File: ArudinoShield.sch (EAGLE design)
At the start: 21 parts, among them IC1 L298

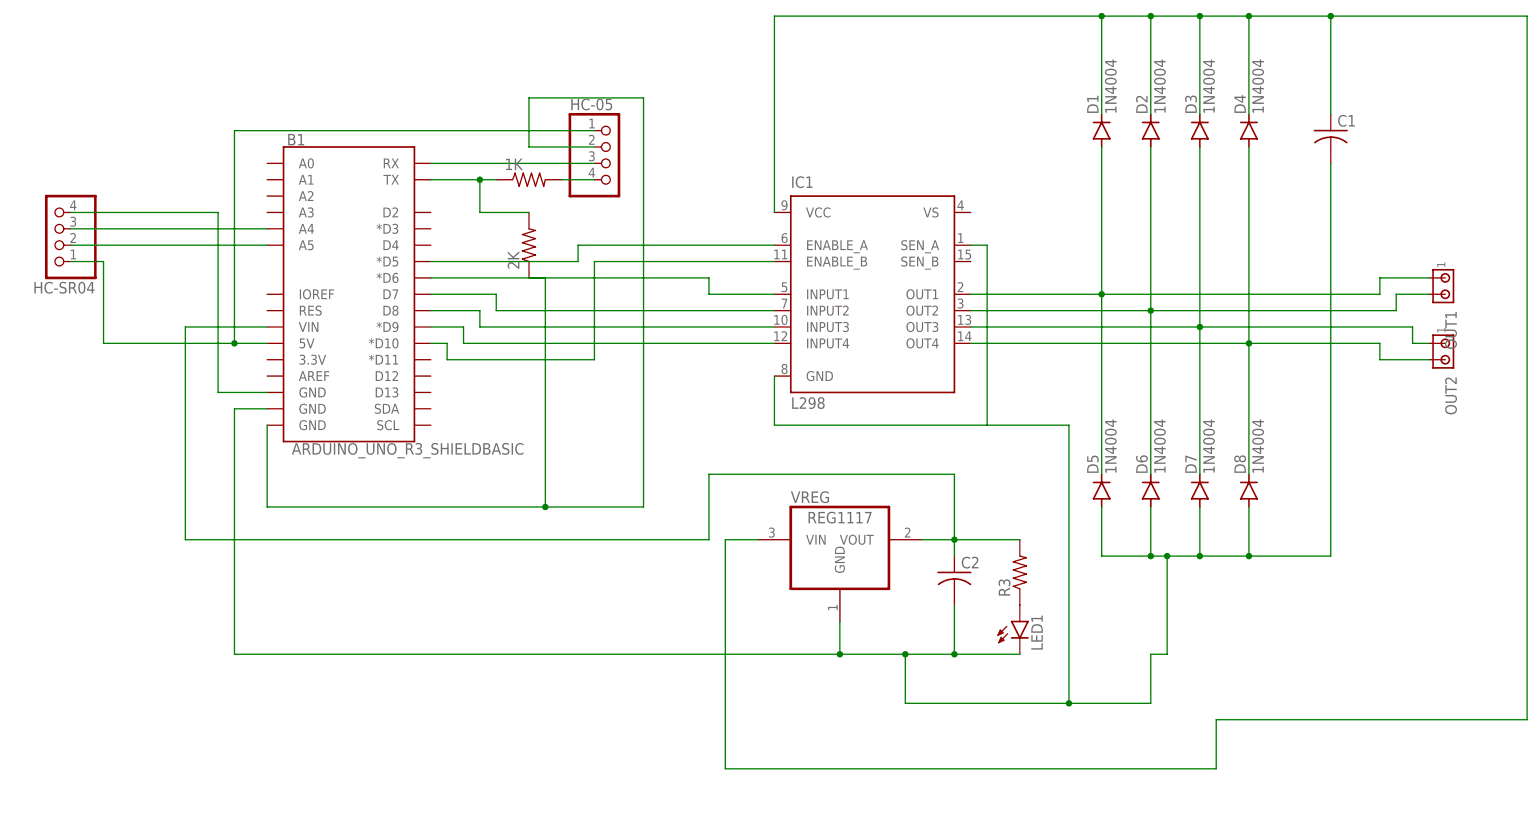
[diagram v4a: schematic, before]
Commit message: added values, updated gitignore for eagle files
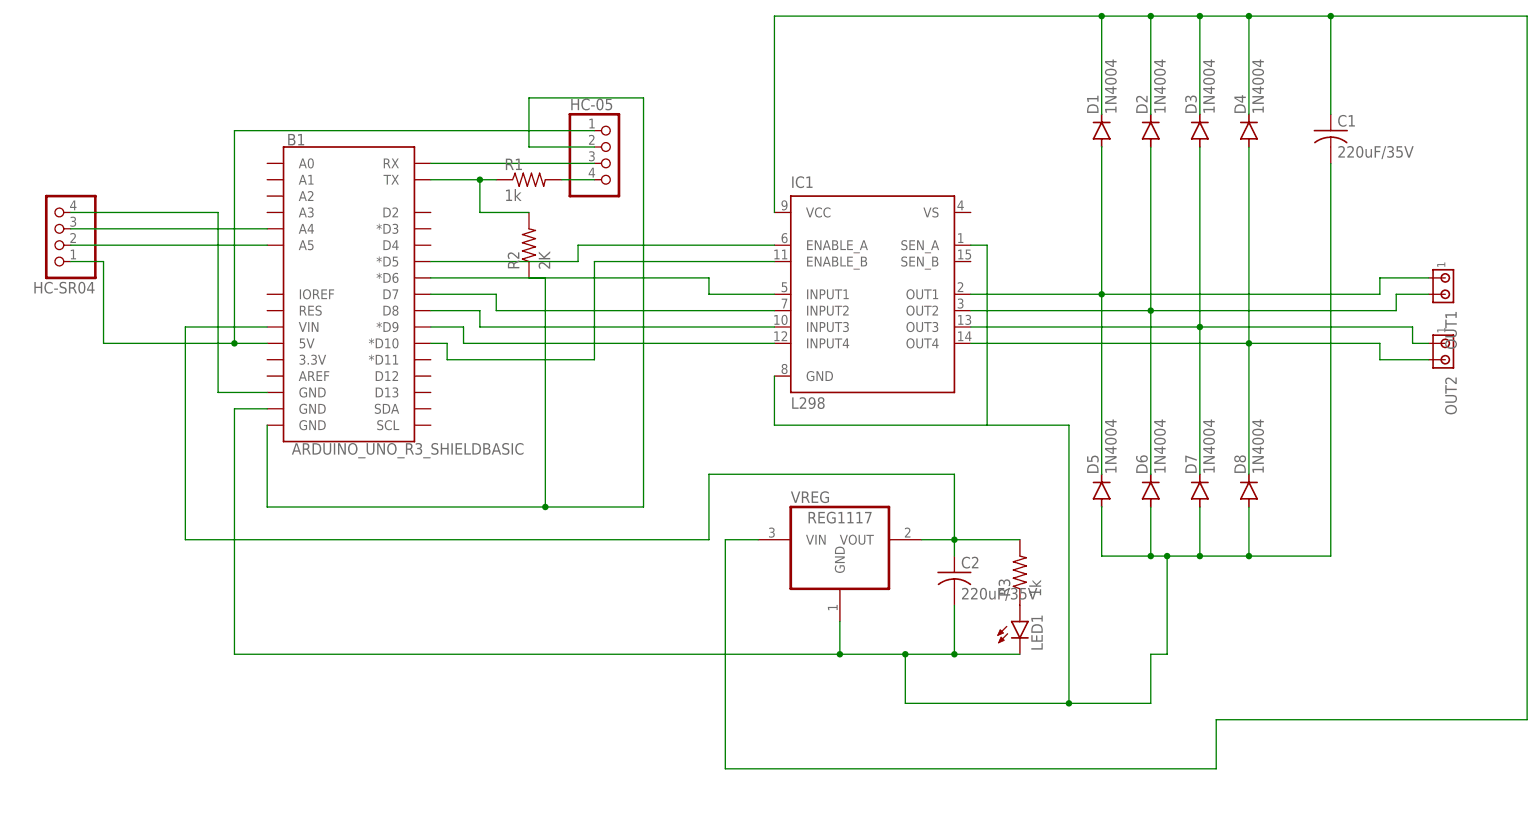
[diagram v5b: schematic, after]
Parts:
- C1, C2: value (none) -> 220uF/35V
- R1, R3: value (none) -> 1k
- R2: value (none) -> 2K
- renumbered 1K to R1, 2K to R2
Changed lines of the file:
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@@
 <part name="HC-SR04" library="pinhead" library_urn="urn:adsk.eagle:library:325" deviceset="PINHD-1X4" device="" package3d_urn="urn:adsk.eagle:package:22407/2"/>
 <part name="HC-05" library="pinhead" library_urn="urn:adsk.eagle:library:325" deviceset="PINHD-1X4" device="" package3d_urn="urn:adsk.eagle:package:22407/2"/>
-<part name="1K" library="adafruit" deviceset="R-US_" device="0207/7"/>
-<part name="2K" library="adafruit" deviceset="R-US_" device="0207/7"/>
+<part name="R1" library="adafruit" deviceset="R-US_" device="0207/7" value="1k"/>
+<part name="R2" library="adafruit" deviceset="R-US_" device="0207/7" value="2K"/>
 <part name="IC1" library="st-microelectronics" library_urn="urn:adsk.eagle:library:368" deviceset="L298" device="" package3d_urn="urn:adsk.eagle:package:26823/1"/>
 <part name="D1" library="diode" library_urn="urn:adsk.eagle:library:210" deviceset="1N4004" device="" package3d_urn="urn:adsk.eagle:package:43336/1"/>
@@
 <part name="OUT1" library="con-amp" library_urn="urn:adsk.eagle:library:127" deviceset="MTA02-156" device="" package3d_urn="urn:adsk.eagle:package:8081562/1"/>
 <part name="OUT2" library="con-amp" library_urn="urn:adsk.eagle:library:127" deviceset="MTA02-156" device="" package3d_urn="urn:adsk.eagle:package:8081562/1"/>
-<part name="C1" library="rcl" library_urn="urn:adsk.eagle:library:334" deviceset="C-US" device="050-024X044" package3d_urn="urn:adsk.eagle:package:23643/1"/>
-<part name="C2" library="rcl" library_urn="urn:adsk.eagle:library:334" deviceset="C-US" device="050-024X044" package3d_urn="urn:adsk.eagle:package:23643/1"/>
-<part name="R3" library="rcl" library_urn="urn:adsk.eagle:library:334" deviceset="R-US_" device="0207/10" package3d_urn="urn:adsk.eagle:package:23491/2"/>
+<part name="C1" library="rcl" library_urn="urn:adsk.eagle:library:334" deviceset="C-US" device="050-024X044" package3d_urn="urn:adsk.eagle:package:23643/1" value="220uF/35V"/>
+<part name="C2" library="rcl" library_urn="urn:adsk.eagle:library:334" deviceset="C-US" device="050-024X044" package3d_urn="urn:adsk.eagle:package:23643/1" value="220uF/35V"/>
+<part name="R3" library="rcl" library_urn="urn:adsk.eagle:library:334" deviceset="R-US_" device="0207/10" package3d_urn="urn:adsk.eagle:package:23491/2" value="1k"/>
 <part name="LED1" library="led" library_urn="urn:adsk.eagle:library:259" deviceset="LED" device="5MM" package3d_urn="urn:adsk.eagle:package:15799/2"/>
 <part name="VREG" library="burr-brown" library_urn="urn:adsk.eagle:library:111" deviceset="REG1117" device="" package3d_urn="urn:adsk.eagle:package:4940/1"/>
@@
 <attribute name="VALUE" x="97.79" y="63.5" size="1.778" layer="96"/>
 </instance>
-<instance part="1K" gate="G$1" x="91.44" y="68.58" smashed="yes">
+<instance part="R1" gate="G$1" x="91.44" y="68.58" smashed="yes">
 <attribute name="NAME" x="87.63" y="70.0786" size="1.778" layer="95"/>
 <attribute name="VALUE" x="87.63" y="65.278" size="1.778" layer="96"/>
 </instance>
-<instance part="2K" gate="G$1" x="91.44" y="58.42" smashed="yes" rot="R90">
+<instance part="R2" gate="G$1" x="91.44" y="58.42" smashed="yes" rot="R90">
 <attribute name="NAME" x="89.9414" y="54.61" size="1.778" layer="95" rot="R90"/>
 <attribute name="VALUE" x="94.742" y="54.61" size="1.778" layer="96" rot="R90"/>
@@
 <wire x1="93.98" y1="17.78" x2="50.8" y2="17.78" width="0.1524" layer="91"/>
 <wire x1="50.8" y1="17.78" x2="50.8" y2="30.48" width="0.1524" layer="91"/>
-<pinref part="2K" gate="G$1" pin="1"/>
+<pinref part="R2" gate="G$1" pin="1"/>
 <wire x1="91.44" y1="53.34" x2="93.98" y2="53.34" width="0.1524" layer="91"/>
 <wire x1="93.98" y1="53.34" x2="93.98" y2="17.78" width="0.1524" layer="91"/>
@@
 <net name="N$11" class="0">
 <segment>
-<pinref part="1K" gate="G$1" pin="1"/>
+<pinref part="R1" gate="G$1" pin="1"/>
 <pinref part="B1" gate="G$1" pin="TX"/>
 <wire x1="86.36" y1="68.58" x2="83.82" y2="68.58" width="0.1524" layer="91"/>
-<pinref part="2K" gate="G$1" pin="2"/>
+<pinref part="R2" gate="G$1" pin="2"/>
 <wire x1="83.82" y1="68.58" x2="76.2" y2="68.58" width="0.1524" layer="91"/>
 <wire x1="91.44" y1="63.5" x2="83.82" y2="63.5" width="0.1524" layer="91"/>
@@
 <net name="N$14" class="0">
 <segment>
-<pinref part="1K" gate="G$1" pin="2"/>
+<pinref part="R1" gate="G$1" pin="2"/>
 <pinref part="HC-05" gate="A" pin="4"/>
 <wire x1="96.52" y1="68.58" x2="101.6" y2="68.58" width="0.1524" layer="91"/>

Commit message: updated schematic for proper pinout from L298 and added supply voltage terminal block
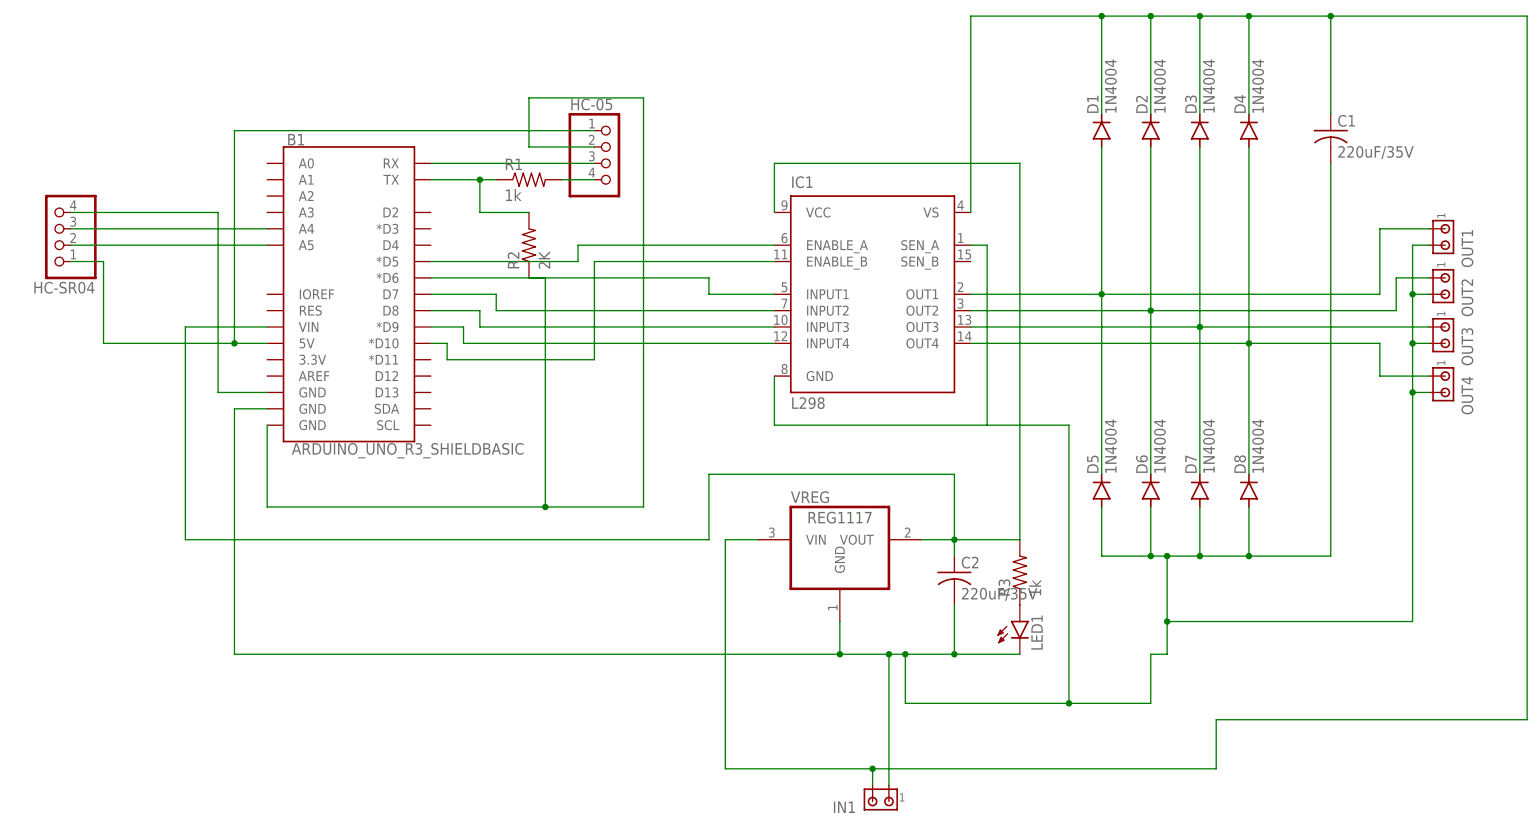
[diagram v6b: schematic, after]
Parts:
- added IN1, OUT3, OUT4: (no value), con-amp:MTA02-156
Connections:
- net N$16: now also OUT2.1; no longer OUT1.2
- net N$17: now also OUT3.1; no longer OUT2.1
- net N$18: now also OUT4.1; no longer OUT2.2
- net N$26: now also IC1.VCC
- net N$29: now also IN1.1, OUT1.2, OUT2.2, OUT3.2, OUT4.2
- net N$31: now also IC1.VS, IN1.2; no longer IC1.VCC
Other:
- moved on the sheet: OUT1, OUT2
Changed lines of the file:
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@@
 <part name="LED1" library="led" library_urn="urn:adsk.eagle:library:259" deviceset="LED" device="5MM" package3d_urn="urn:adsk.eagle:package:15799/2"/>
 <part name="VREG" library="burr-brown" library_urn="urn:adsk.eagle:library:111" deviceset="REG1117" device="" package3d_urn="urn:adsk.eagle:package:4940/1"/>
+<part name="IN1" library="con-amp" library_urn="urn:adsk.eagle:library:127" deviceset="MTA02-156" device="" package3d_urn="urn:adsk.eagle:package:8081562/1"/>
+<part name="OUT3" library="con-amp" library_urn="urn:adsk.eagle:library:127" deviceset="MTA02-156" device="" package3d_urn="urn:adsk.eagle:package:8081562/1"/>
+<part name="OUT4" library="con-amp" library_urn="urn:adsk.eagle:library:127" deviceset="MTA02-156" device="" package3d_urn="urn:adsk.eagle:package:8081562/1"/>
 </parts>
 <sheets>
@@
 <attribute name="VALUE" x="205.5114" y="22.86" size="1.778" layer="96" rot="R90"/>
 </instance>
-<instance part="OUT1" gate="G$1" x="233.68" y="53.34" smashed="yes" rot="R270">
-<attribute name="NAME" x="233.68" y="48.26" size="1.778" layer="95" rot="R270"/>
+<instance part="OUT1" gate="G$1" x="233.68" y="60.96" smashed="yes" rot="R270">
+<attribute name="NAME" x="236.22" y="60.96" size="1.778" layer="95" rot="R270"/>
+<attribute name="VALUE" x="229.87" y="55.88" size="1.778" layer="96" rot="R270"/>
+</instance>
+<instance part="OUT2" gate="G$1" x="233.68" y="53.34" smashed="yes" rot="R270">
+<attribute name="NAME" x="236.22" y="53.34" size="1.778" layer="95" rot="R270"/>
 <attribute name="VALUE" x="229.87" y="48.26" size="1.778" layer="96" rot="R270"/>
-</instance>
-<instance part="OUT2" gate="G$1" x="233.68" y="43.18" smashed="yes" rot="R270">
-<attribute name="NAME" x="233.68" y="38.1" size="1.778" layer="95" rot="R270"/>
-<attribute name="VALUE" x="229.87" y="38.1" size="1.778" layer="96" rot="R270"/>
 </instance>
 <instance part="C1" gate="G$1" x="215.9" y="76.2" smashed="yes">
@@
 <attribute name="NAME" x="132.08" y="18.415" size="1.778" layer="95" ratio="10"/>
 <attribute name="VALUE" x="134.62" y="15.24" size="1.778" layer="96" ratio="10"/>
+</instance>
+<instance part="IN1" gate="G$1" x="147.32" y="-27.94" smashed="yes" rot="R180">
+<attribute name="NAME" x="142.24" y="-27.94" size="1.778" layer="95" rot="R180"/>
+<attribute name="VALUE" x="142.24" y="-24.13" size="1.778" layer="96" rot="R180"/>
+</instance>
+<instance part="OUT3" gate="G$1" x="233.68" y="45.72" smashed="yes" rot="R270">
+<attribute name="NAME" x="236.22" y="45.72" size="1.778" layer="95" rot="R270"/>
+<attribute name="VALUE" x="229.87" y="40.64" size="1.778" layer="96" rot="R270"/>
+</instance>
+<instance part="OUT4" gate="G$1" x="233.68" y="38.1" smashed="yes" rot="R270">
+<attribute name="NAME" x="236.22" y="38.1" size="1.778" layer="95" rot="R270"/>
+<attribute name="VALUE" x="229.87" y="33.02" size="1.778" layer="96" rot="R270"/>
 </instance>
 </instances>
@@
 <wire x1="180.34" y1="73.66" x2="180.34" y2="50.8" width="0.1524" layer="91"/>
 <pinref part="OUT1" gate="G$1" pin="1"/>
-<wire x1="231.14" y1="53.34" x2="223.52" y2="53.34" width="0.1524" layer="91"/>
-<wire x1="223.52" y1="53.34" x2="223.52" y2="50.8" width="0.1524" layer="91"/>
+<wire x1="223.52" y1="50.8" x2="223.52" y2="60.96" width="0.1524" layer="91"/>
+<wire x1="223.52" y1="60.96" x2="231.14" y2="60.96" width="0.1524" layer="91"/>
 </segment>
 </net>
@@
 <pinref part="D2" gate="1" pin="A"/>
 <wire x1="187.96" y1="73.66" x2="187.96" y2="48.26" width="0.1524" layer="91"/>
-<pinref part="OUT1" gate="G$1" pin="2"/>
-<wire x1="231.14" y1="50.8" x2="226.06" y2="50.8" width="0.1524" layer="91"/>
-<wire x1="226.06" y1="50.8" x2="226.06" y2="48.26" width="0.1524" layer="91"/>
+<pinref part="OUT2" gate="G$1" pin="1"/>
+<wire x1="226.06" y1="48.26" x2="226.06" y2="53.34" width="0.1524" layer="91"/>
+<wire x1="226.06" y1="53.34" x2="231.14" y2="53.34" width="0.1524" layer="91"/>
 </segment>
 </net>
@@
 <wire x1="160.02" y1="45.72" x2="195.58" y2="45.72" width="0.1524" layer="91"/>
 <pinref part="D7" gate="1" pin="C"/>
-<wire x1="195.58" y1="45.72" x2="228.6" y2="45.72" width="0.1524" layer="91"/>
+<wire x1="195.58" y1="45.72" x2="231.14" y2="45.72" width="0.1524" layer="91"/>
 <wire x1="195.58" y1="22.86" x2="195.58" y2="45.72" width="0.1524" layer="91"/>
 <junction x="195.58" y="45.72"/>
 <pinref part="D3" gate="1" pin="A"/>
 <wire x1="195.58" y1="73.66" x2="195.58" y2="45.72" width="0.1524" layer="91"/>
-<pinref part="OUT2" gate="G$1" pin="1"/>
-<wire x1="231.14" y1="43.18" x2="228.6" y2="43.18" width="0.1524" layer="91"/>
-<wire x1="228.6" y1="43.18" x2="228.6" y2="45.72" width="0.1524" layer="91"/>
+<pinref part="OUT3" gate="G$1" pin="1"/>
 </segment>
 </net>
@@
 <pinref part="D4" gate="1" pin="A"/>
 <wire x1="203.2" y1="73.66" x2="203.2" y2="43.18" width="0.1524" layer="91"/>
-<pinref part="OUT2" gate="G$1" pin="2"/>
-<wire x1="231.14" y1="40.64" x2="223.52" y2="40.64" width="0.1524" layer="91"/>
-<wire x1="223.52" y1="40.64" x2="223.52" y2="43.18" width="0.1524" layer="91"/>
+<pinref part="OUT4" gate="G$1" pin="1"/>
+<wire x1="223.52" y1="43.18" x2="223.52" y2="38.1" width="0.1524" layer="91"/>
+<wire x1="223.52" y1="38.1" x2="231.14" y2="38.1" width="0.1524" layer="91"/>
 </segment>
 </net>
@@
 <segment>
 <pinref part="R3" gate="G$1" pin="2"/>
-<wire x1="167.64" y1="12.7" x2="157.48" y2="12.7" width="0.1524" layer="91"/>
 <pinref part="C2" gate="G$1" pin="1"/>
 <wire x1="157.48" y1="12.7" x2="152.4" y2="12.7" width="0.1524" layer="91"/>
@@
 <wire x1="119.38" y1="22.86" x2="157.48" y2="22.86" width="0.1524" layer="91"/>
 <wire x1="157.48" y1="22.86" x2="157.48" y2="12.7" width="0.1524" layer="91"/>
+<wire x1="157.48" y1="12.7" x2="167.64" y2="12.7" width="0.1524" layer="91"/>
+<wire x1="167.64" y1="12.7" x2="167.64" y2="71.12" width="0.1524" layer="91"/>
+<wire x1="167.64" y1="71.12" x2="129.54" y2="71.12" width="0.1524" layer="91"/>
+<pinref part="IC1" gate="L298" pin="VCC"/>
+<wire x1="129.54" y1="71.12" x2="129.54" y2="63.5" width="0.1524" layer="91"/>
 </segment>
 </net>
@@
 <pinref part="C2" gate="G$1" pin="2"/>
 <wire x1="157.48" y1="-5.08" x2="149.86" y2="-5.08" width="0.1524" layer="91"/>
-<wire x1="149.86" y1="-5.08" x2="139.7" y2="-5.08" width="0.1524" layer="91"/>
+<wire x1="149.86" y1="-5.08" x2="147.32" y2="-5.08" width="0.1524" layer="91"/>
+<wire x1="147.32" y1="-5.08" x2="139.7" y2="-5.08" width="0.1524" layer="91"/>
 <wire x1="157.48" y1="2.54" x2="157.48" y2="-5.08" width="0.1524" layer="91"/>
 <junction x="157.48" y="-5.08"/>
@@
 <wire x1="215.9" y1="10.16" x2="203.2" y2="10.16" width="0.1524" layer="91"/>
 <junction x="203.2" y="10.16"/>
-<wire x1="190.5" y1="-5.08" x2="190.5" y2="10.16" width="0.1524" layer="91"/>
+<wire x1="190.5" y1="-5.08" x2="190.5" y2="0" width="0.1524" layer="91"/>
 <junction x="190.5" y="10.16"/>
+<wire x1="190.5" y1="0" x2="190.5" y2="10.16" width="0.1524" layer="91"/>
 <wire x1="162.56" y1="30.48" x2="175.26" y2="30.48" width="0.1524" layer="91"/>
 <wire x1="175.26" y1="30.48" x2="175.26" y2="-12.7" width="0.1524" layer="91"/>
@@
 <wire x1="45.72" y1="-5.08" x2="139.7" y2="-5.08" width="0.1524" layer="91"/>
 <junction x="139.7" y="-5.08"/>
+<pinref part="IN1" gate="G$1" pin="1"/>
+<wire x1="147.32" y1="-25.4" x2="147.32" y2="-5.08" width="0.1524" layer="91"/>
+<junction x="147.32" y="-5.08"/>
+<pinref part="OUT1" gate="G$1" pin="2"/>
+<wire x1="231.14" y1="58.42" x2="228.6" y2="58.42" width="0.1524" layer="91"/>
+<wire x1="228.6" y1="58.42" x2="228.6" y2="50.8" width="0.1524" layer="91"/>
+<wire x1="228.6" y1="50.8" x2="228.6" y2="43.18" width="0.1524" layer="91"/>
+<wire x1="228.6" y1="43.18" x2="228.6" y2="35.56" width="0.1524" layer="91"/>
+<wire x1="228.6" y1="35.56" x2="228.6" y2="0" width="0.1524" layer="91"/>
+<wire x1="228.6" y1="0" x2="190.5" y2="0" width="0.1524" layer="91"/>
+<junction x="190.5" y="0"/>
+<pinref part="OUT2" gate="G$1" pin="2"/>
+<wire x1="231.14" y1="50.8" x2="228.6" y2="50.8" width="0.1524" layer="91"/>
+<junction x="228.6" y="50.8"/>
+<pinref part="OUT3" gate="G$1" pin="2"/>
+<wire x1="231.14" y1="43.18" x2="228.6" y2="43.18" width="0.1524" layer="91"/>
+<junction x="228.6" y="43.18"/>
+<pinref part="OUT4" gate="G$1" pin="2"/>
+<wire x1="231.14" y1="35.56" x2="228.6" y2="35.56" width="0.1524" layer="91"/>
+<junction x="228.6" y="35.56"/>
 </segment>
 </net>
@@
 <segment>
 <wire x1="198.12" y1="-15.24" x2="198.12" y2="-22.86" width="0.1524" layer="91"/>
-<wire x1="198.12" y1="-22.86" x2="121.92" y2="-22.86" width="0.1524" layer="91"/>
+<wire x1="198.12" y1="-22.86" x2="144.78" y2="-22.86" width="0.1524" layer="91"/>
+<wire x1="144.78" y1="-22.86" x2="121.92" y2="-22.86" width="0.1524" layer="91"/>
 <wire x1="121.92" y1="-22.86" x2="121.92" y2="12.7" width="0.1524" layer="91"/>
 <wire x1="198.12" y1="-15.24" x2="246.38" y2="-15.24" width="0.1524" layer="91"/>
@@
 <wire x1="187.96" y1="78.74" x2="187.96" y2="93.98" width="0.1524" layer="91"/>
 <junction x="187.96" y="93.98"/>
-<pinref part="IC1" gate="L298" pin="VCC"/>
-<wire x1="129.54" y1="63.5" x2="129.54" y2="93.98" width="0.1524" layer="91"/>
-<wire x1="129.54" y1="93.98" x2="180.34" y2="93.98" width="0.1524" layer="91"/>
 <junction x="180.34" y="93.98"/>
+<wire x1="160.02" y1="93.98" x2="180.34" y2="93.98" width="0.1524" layer="91"/>
 <wire x1="246.38" y1="-15.24" x2="246.38" y2="93.98" width="0.1524" layer="91"/>
 <wire x1="246.38" y1="93.98" x2="215.9" y2="93.98" width="0.1524" layer="91"/>
@@
 <pinref part="VREG" gate="G$1" pin="VIN"/>
 <wire x1="127" y1="12.7" x2="121.92" y2="12.7" width="0.1524" layer="91"/>
-</segment>
-</net>
+<pinref part="IC1" gate="L298" pin="VS"/>
+<wire x1="160.02" y1="63.5" x2="160.02" y2="93.98" width="0.1524" layer="91"/>
+<pinref part="IN1" gate="G$1" pin="2"/>
+<wire x1="144.78" y1="-25.4" x2="144.78" y2="-22.86" width="0.1524" layer="91"/>
+<junction x="144.78" y="-22.86"/>
+</segment>
+</net>
